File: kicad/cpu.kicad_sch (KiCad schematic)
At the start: 7 parts, among them SW1 RESET, U1 W65C816S, U2 74HC573, U3 ATF22V10C 816DEC02, X1 12MHz

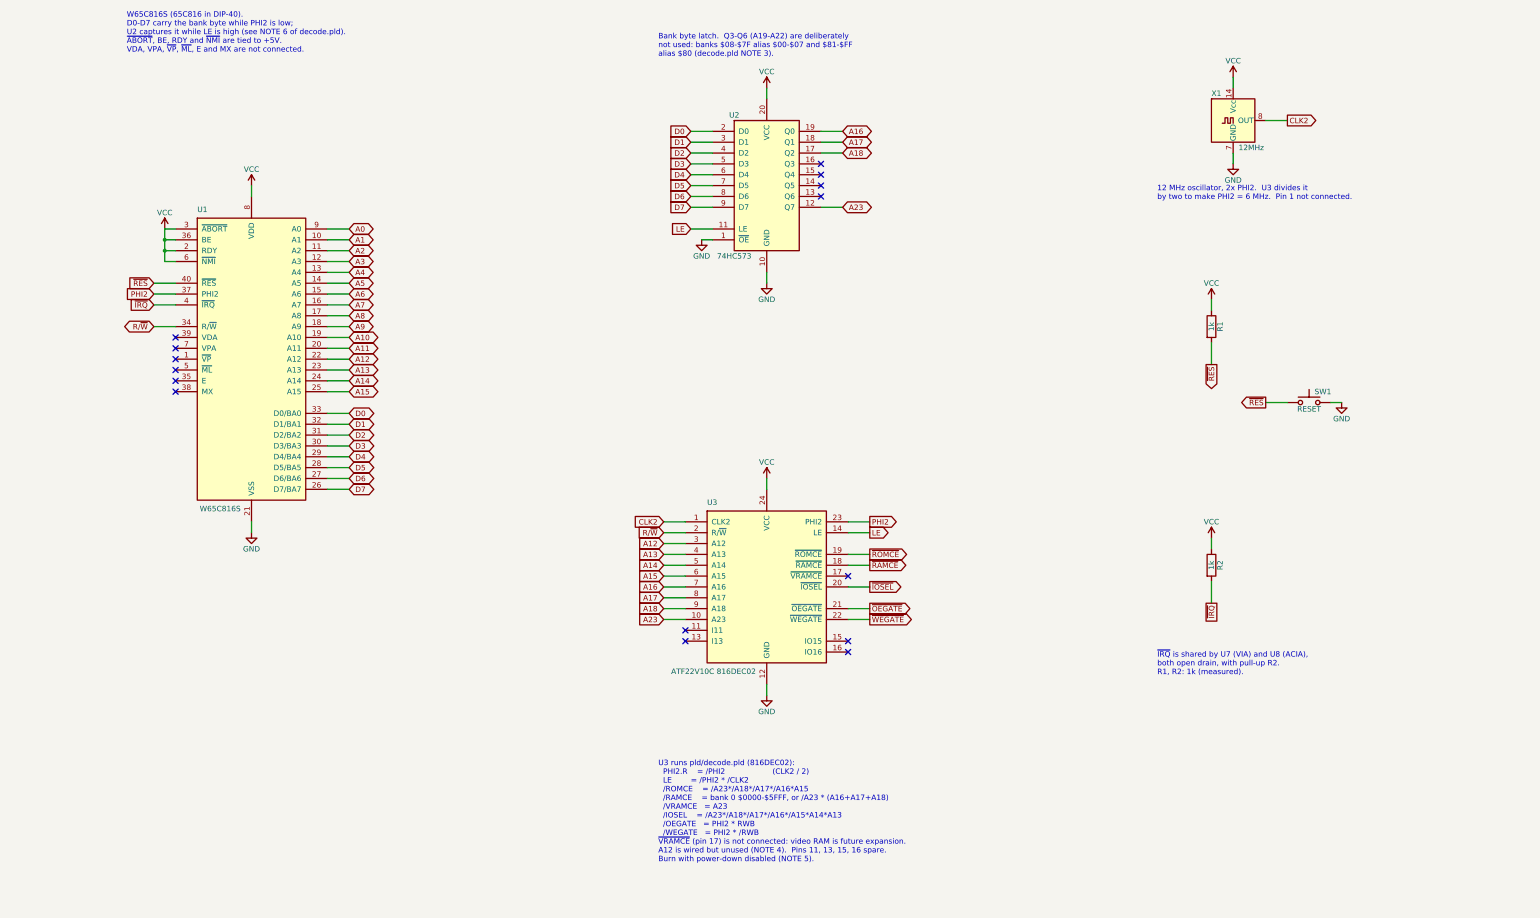
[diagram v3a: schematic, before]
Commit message: Schematic rev 2: prepare the design for a 4-layer PCB
Keeps the breadboard's parts and logic and adds what a board needs.

- RDY, NMI, ABORT and BE get 3.3k pull-ups instead of hard ties to +5V
  (RDY is bidirectional; WAI drives it low).
- VDA and VPA go to GAL pins 11 and 13. New pld/decode03.pld (816DEC03)
  qualifies /IOSEL with VDA + VPA so internal-operation cycles cannot
  read and clear ACIA/VIA registers. decode.pld (816DEC02) stays for the
  breadboard.
- PHI2 from the GAL can be routed through a 74ACT08 buffer via JP2
  (default: direct, as built). Timing in decode03.pld NOTE 8.
- Clock source jumper JP1 and external clock header J5.
- New power sheet: USB-C (power only) or bench terminal via JP4, power
  switch, polyfuse, P-FET reverse-polarity protection, 47uF bulk, power
  LED, and 100nF decoupling per package.
- New expansion sheet: 2x30 bus header (address, latched bank byte,
  data, control, spare I/O slots), 2x12 VIA header, LED disconnect
  jumper, test points, mounting holes.
- Footprints on every part; socket footprints for all ICs.

ERC (KiCad 9.0.4 kicad-cli): 0 errors, 0 warnings. Both PLD files
assemble with Galette 0.3.0.

Co-Authored-By: Claude Opus 5.5 <noreply@anthropic.com>
Claude-Session: https://claude.ai/code/session_01WF6ESyzfg6uQED2DRD2W4Z
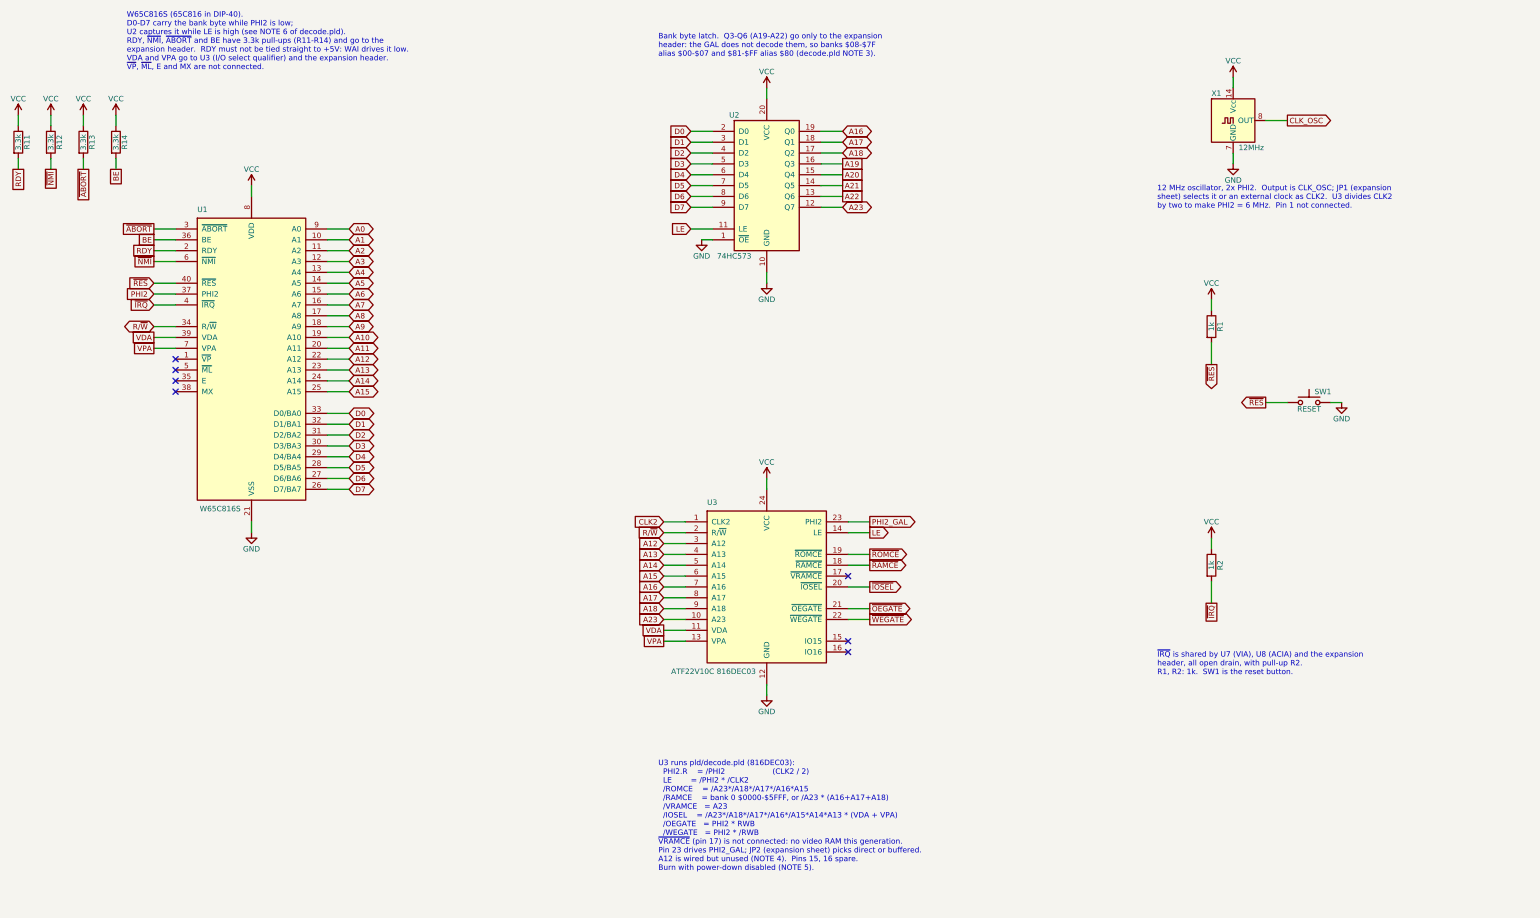
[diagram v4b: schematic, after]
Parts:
- added R11, R12, R13, R14: 3.3k, Resistor_THT:R_Axial_DIN0207_L6.3mm_D2.5mm_P7.62mm_Horizontal, symbol be6502:R
- R1, R2: footprint (none) -> Resistor_THT:R_Axial_DIN0207_L6.3mm_D2.5mm_P7.62mm_Horizontal
- SW1: footprint (none) -> Button_Switch_THT:SW_PUSH_6mm
- U1: footprint Package_DIP:DIP-40_W15.24mm -> Package_DIP:DIP-40_W15.24mm_Socket
- U2: footprint Package_DIP:DIP-20_W7.62mm -> Package_DIP:DIP-20_W7.62mm_Socket
- U3: value ATF22V10C 816DEC02 -> ATF22V10C 816DEC03; footprint Package_DIP:DIP-24_W7.62mm -> Package_DIP:DIP-24_W7.62mm_Socket; symbol be6502:ATF22V10C-816DEC02 -> be6502:ATF22V10C-816DEC03
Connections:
- net CLK2: no longer X1.8 (OUT)
- net PHI2: no longer U3.23 (PHI2)
- net VCC: now also R11.1, R12.1, R13.1, R14.1; no longer U1.2 (RDY), U1.3 (~{ABORT}), U1.36 (BE), U1.6 (~{NMI})
- net VDA: now reaches U1.39 (VDA)
- net VDA: now also U3.11 (VDA)
- net VPA: now reaches U1.7 (VPA)
- net VPA: now also U3.13 (VPA)
- net A22: now reaches U2.13 (Q6)
- net A21: now reaches U2.14 (Q5)
- net A20: now reaches U2.15 (Q4)
- net A19: now reaches U2.16 (Q3)
- new net BE: R14.2, U1.36 (BE)
- new net CLK_OSC: X1.8 (OUT)
- new net PHI2_GAL: U3.23 (PHI2)
- new net RDY: R11.2, U1.2 (RDY)
- new net ~{ABORT}: R13.2, U1.3 (~{ABORT})
- new net ~{NMI}: R12.2, U1.6 (~{NMI})
- no-connect marks 15 -> 7
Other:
- note added: "12 MHz oscillator, 2x PHI2. Output is CLK_OSC; JP1 (expansion sheet) selects it or an external clock as CLK2. U3 divides CLK2 by two to make PHI2 = 6 MHz. Pin 1 not connected."
- note added: "Bank byte latch. Q3-Q6 (A19-A22) go only to the expansion header: the GAL does not decode them, so banks $08-$7F alias $00-$07 and $81-$FF alias $80 (decode.pld NOTE 3)."
- note added: "U3 runs pld/decode.pld (816DEC03): PHI2.R = /PHI2 (CLK2 / 2) LE = /PHI2 * /CLK2 /ROMCE = /A23*/A18*/A17*/A16*A15 /RAMCE = bank 0 $0000-$5FFF, or /A23 * (A16+A17+A18) /VRAMCE = A23 /IOSEL = /A23*/A18*/A17*/A16*/A15*A14*A13 * (VDA + VPA) /OEGATE = PHI2 * RWB /WEGATE = PHI2 * /RWB ~{VRAMCE} (pin 17) is not connected: no video RAM this generation. Pin 23 drives PHI2_GAL; JP2 (expansion sheet) picks d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"
- note added: "W65C816S (65C816 in DIP-40). D0-D7 carry the bank byte while PHI2 is low; U2 captures it while LE is high (see NOTE 6 of decode.pld). RDY, ~{NMI}, ~{ABORT} and BE have 3.3k pull-ups (R11-R14) and go to the expansion header. RDY must not be tied straight to +5V: WAI drives it low. VDA and VPA go to U3 (I/O select qualifier) and the expansion header. ~{VP}, ~{ML}, E and MX are not connected."
- note added: "~{IRQ} is shared by U7 (VIA), U8 (ACIA) and the expansion header, all open drain, with pull-up R2. R1, R2: 1k. SW1 is the reset button."
- note removed: "12 MHz oscillator, 2x PHI2. U3 divides it by two to make PHI2 = 6 MHz. Pin 1 not connected."
- note removed: "Bank byte latch. Q3-Q6 (A19-A22) are deliberately not used: banks $08-$7F alias $00-$07 and $81-$FF alias $80 (decode.pld NOTE 3)."
- note removed: "U3 runs pld/decode.pld (816DEC02): PHI2.R = /PHI2 (CLK2 / 2) LE = /PHI2 * /CLK2 /ROMCE = /A23*/A18*/A17*/A16*A15 /RAMCE = bank 0 $0000-$5FFF, or /A23 * (A16+A17+A18) /VRAMCE = A23 /IOSEL = /A23*/A18*/A17*/A16*/A15*A14*A13 /OEGATE = PHI2 * RWB /WEGATE = PHI2 * /RWB ~{VRAMCE} (pin 17) is not connected: video RAM is future expansion. A12 is wired but unused (NOTE 4). Pins 11, 13, 15, 16 spare. Burn 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"
- note removed: "W65C816S (65C816 in DIP-40). D0-D7 carry the bank byte while PHI2 is low; U2 captures it while LE is high (see NOTE 6 of decode.pld). ~{ABORT}, BE, RDY and ~{NMI} are tied to +5V. VDA, VPA, ~{VP}, ~{ML}, E and MX are not connected."
- note removed: "~{IRQ} is shared by U7 (VIA) and U8 (ACIA), both open drain, with pull-up R2. R1, R2: 1k (measured)."

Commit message: Add DS1813-5 reset supervisor; RDY pull-up back to 1k
U11 (TO-92) gives a power-on reset and debounces SW1; its open-drain RST
shares ~RES with the button and the expansion header. R1 becomes 10k.
R11 (RDY pull-up) is 1k to match the breadboard. ERC still clean.

Co-Authored-By: Claude Opus 5.5 <noreply@anthropic.com>
Claude-Session: https://claude.ai/code/session_01WF6ESyzfg6uQED2DRD2W4Z
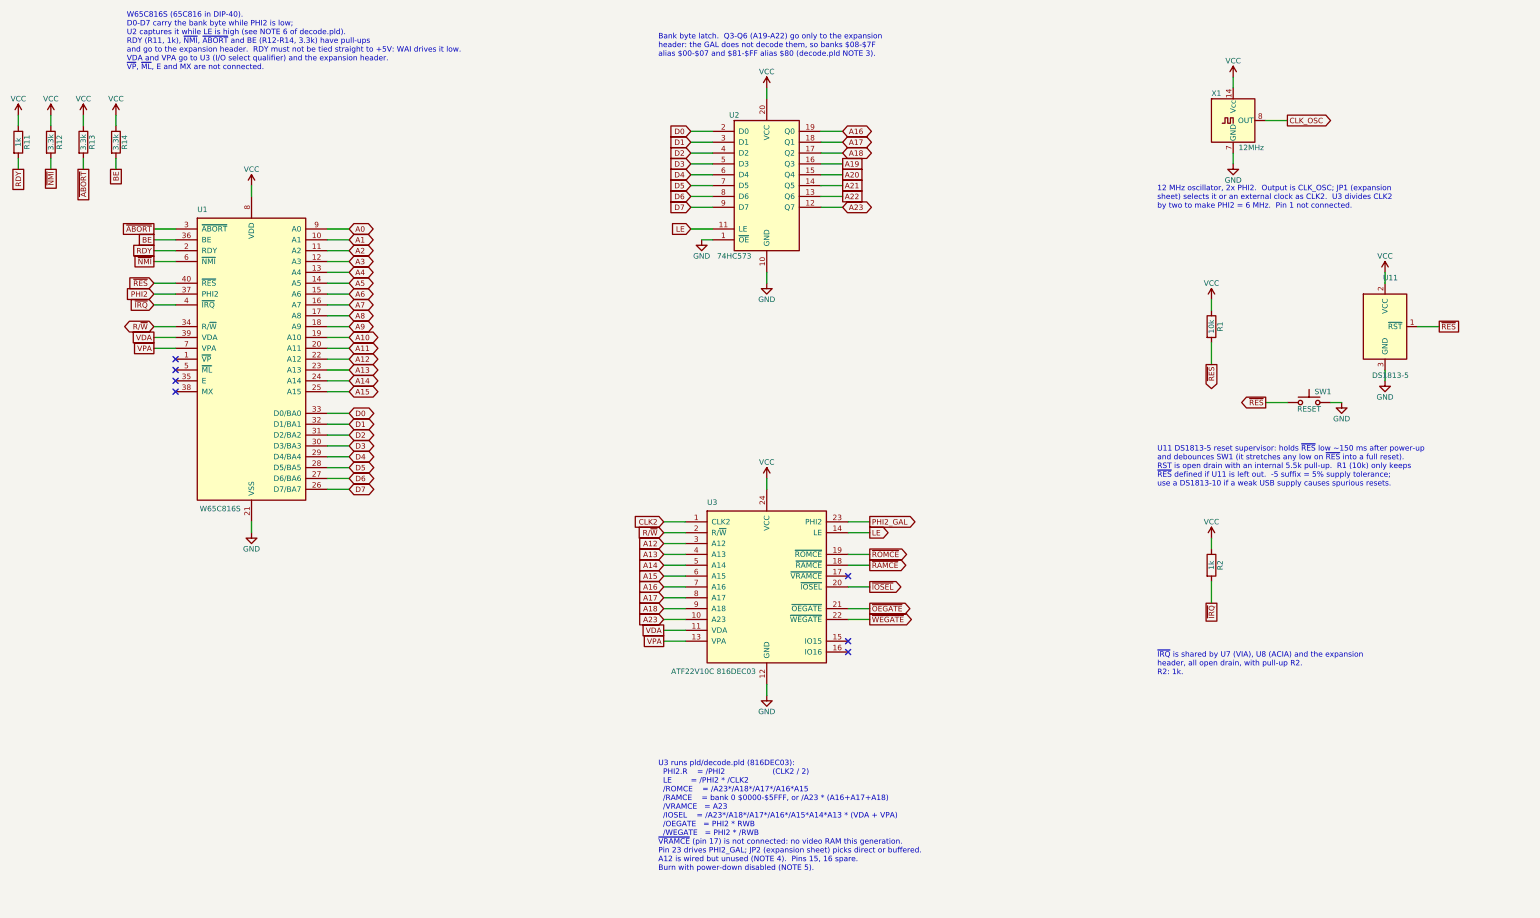
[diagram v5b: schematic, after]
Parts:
- added U11: DS1813-5, Package_TO_SOT_THT:TO-92_Inline, symbol be6502:DS1813
- R1: value 1k -> 10k
- R11: value 3.3k -> 1k
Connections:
- net GND: now also U11.3 (GND)
- net VCC: now also U11.2 (VCC)
- net ~{RES}: now also U11.1 (~{RST})
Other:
- note added: "U11 DS1813-5 reset supervisor: holds ~{RES} low ~150 ms after power-up and debounces SW1 (it stretches any low on ~{RES} into a full reset). RST is open drain with an internal 5.5k pull-up. R1 (10k) only keeps ~{RES} defined if U11 is left out. -5 suffix = 5% supply tolerance; use a DS1813-10 if a weak USB supply causes spurious resets."
- note added: "W65C816S (65C816 in DIP-40). D0-D7 carry the bank byte while PHI2 is low; U2 captures it while LE is high (see NOTE 6 of decode.pld). RDY (R11, 1k), ~{NMI}, ~{ABORT} and BE (R12-R14, 3.3k) have pull-ups and go to the expansion header. RDY must not be tied straight to +5V: WAI drives it low. VDA and VPA go to U3 (I/O select qualifier) and the expansion header. ~{VP}, ~{ML}, E and MX are not connec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"
- note added: "~{IRQ} is shared by U7 (VIA), U8 (ACIA) and the expansion header, all open drain, with pull-up R2. R2: 1k."
- note removed: "W65C816S (65C816 in DIP-40). D0-D7 carry the bank byte while PHI2 is low; U2 captures it while LE is high (see NOTE 6 of decode.pld). RDY, ~{NMI}, ~{ABORT} and BE have 3.3k pull-ups (R11-R14) and go to the expansion header. RDY must not be tied straight to +5V: WAI drives it low. VDA and VPA go to U3 (I/O select qualifier) and the expansion header. ~{VP}, ~{ML}, E and MX are not connected."
- note removed: "~{IRQ} is shared by U7 (VIA), U8 (ACIA) and the expansion header, all open drain, with pull-up R2. R1, R2: 1k. SW1 is the reset button."
